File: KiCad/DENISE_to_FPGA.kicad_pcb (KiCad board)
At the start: 2 copper layers, 76.7 x 29.5 mm, 17 parts, among them J1 Conn_01x02, J2 Conn_01x02, J3 Conn_01x40, U1 LM1117-3.3, U2 74LVC245A, U3 74LVC245A, U4 74LVC1G86, U5 Denise_MB_PinHeader

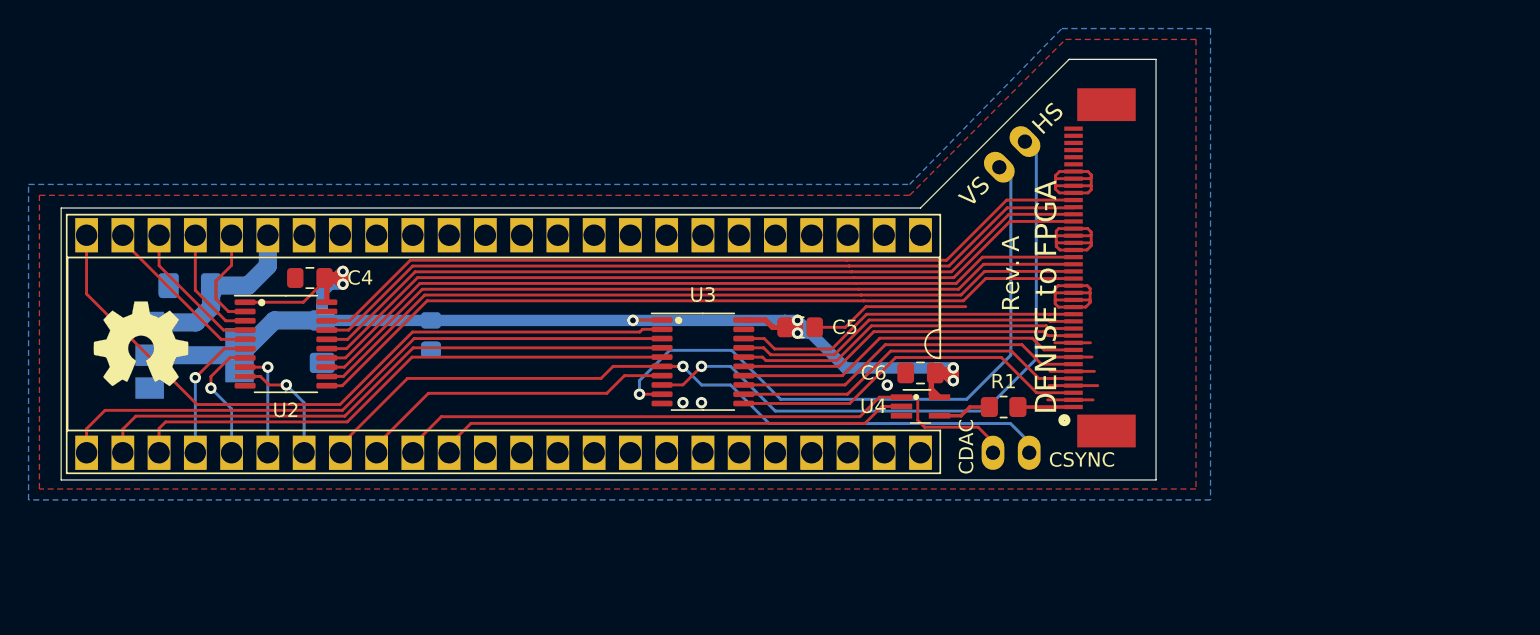
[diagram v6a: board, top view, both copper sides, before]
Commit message: Updated design with a 74LVC162244ADGG, changed PCB size and TH-pins
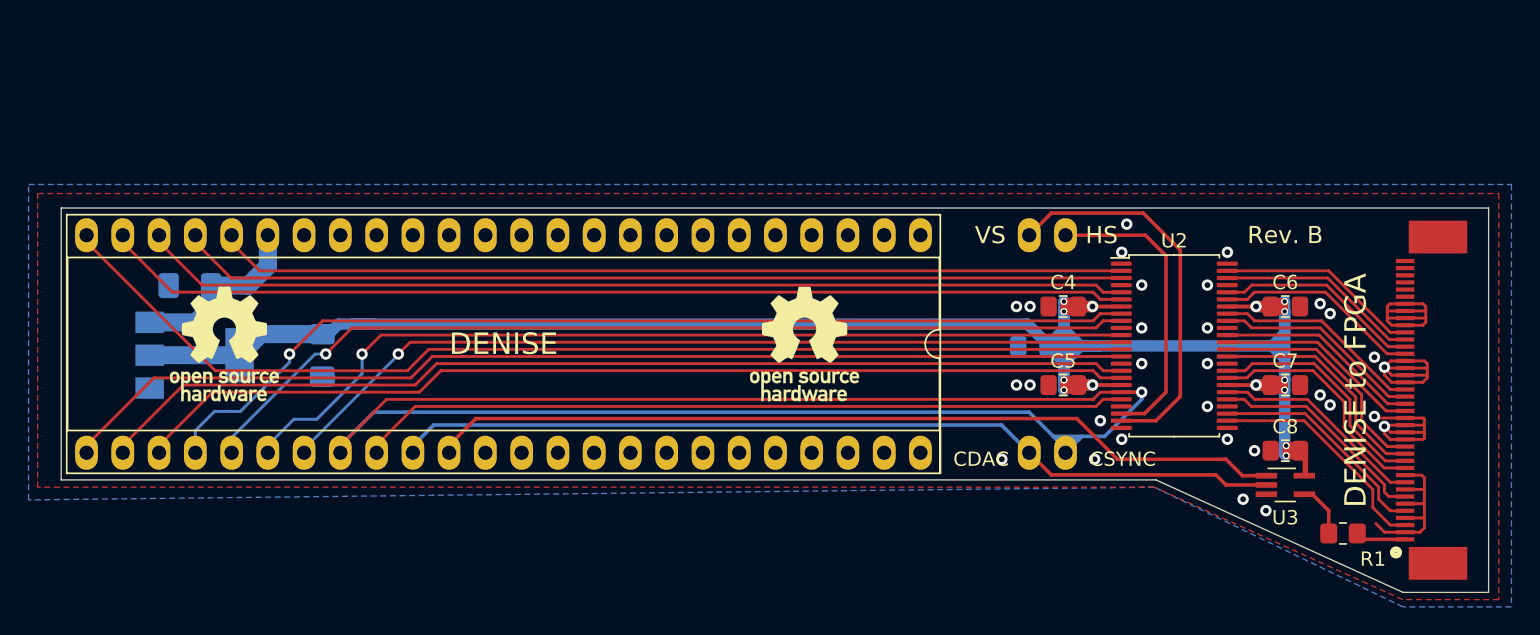
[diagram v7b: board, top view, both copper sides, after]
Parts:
- removed the REF** at (133.3, 95.8)
- removed the U4 at (188.0, 100.1)
- added C7: 0.1uF, DENISE_to_FPGA:C_0805_2012Metric_Pad1.15x1.4mm_HandSolder, F.Cu at (213.5, 98.6)
- added C8: 0.1uF, DENISE_to_FPGA:C_0805_2012Metric_Pad1.15x1.4mm_HandSolder, F.Cu at (213.5, 103.2)
- added REF**: OSHW-Logo_7.5x8mm_SilkScreen, Symbol:OSHW-Logo_7.5x8mm_SilkScreen, F.Cu at (179.8, 95.8)
- added REF**: OSHW-Logo_7.5x8mm_SilkScreen, Symbol:OSHW-Logo_7.5x8mm_SilkScreen, F.Cu at (139.2, 95.8)
- C3: value 0.1uF -> 1uF
- C4, C5: footprint Capacitor_SMD:C_0805_2012Metric_Pad1.15x1.40mm_HandSolder -> DENISE_to_FPGA:C_0805_2012Metric_Pad1.15x1.4mm_HandSolder
- C6: footprint Capacitor_SMD:C_0805_2012Metric_Pad1.18x1.45mm_HandSolder -> DENISE_to_FPGA:C_0805_2012Metric_Pad1.15x1.4mm_HandSolder
- U2: value 74LVC245A -> 74LVC162244A; footprint Package_SO:TSSOP-20_4.4x6.5mm_P0.65mm -> Package_SO:TSSOP-48_6.1x12.5mm_P0.5mm
- U3: value 74LVC245A -> 74LVC1G86; footprint Package_SO:TSSOP-20_4.4x6.5mm_P0.65mm -> Package_TO_SOT_SMD:SOT-353_SC-70-5_Handsoldering
- moved U2 62.2 mm to (205.7, 95.9)
- moved C4 52.8 mm to (198.0, 93.1)
- moved C3 42.2 mm to (195.8, 95.9), turned to 0 degrees
- moved U3 41.7 mm to (213.5, 105.6)
- moved C6 26.0 mm to (213.5, 93.1), turned to 180 degrees
- moved R1 25.4 mm to (217.6, 109.0)
- moved J3 25.0 mm to (223.8, 99.7)
- moved REF** 24.9 mm to (220.4, 98.9)
- moved C5 18.9 mm to (198.0, 98.6), turned to 0 degrees
- moved J2 5.20 mm to (195.6, 88.1), turned to 90 degrees
- moved J1 2.54 mm to (198.1, 103.4)
- moved C2 0.96 mm to (146.1, 96.6)
- renumbered U5 to U4
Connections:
- U2 pad 1: 3V3 -> GND
- U2 pad 11: G3_3V3 -> G2
- U2 pad 12: G2_3V3 -> G3
- U2 pad 13: G1_3V3 -> B0
- U2 pad 14: G0_3V3 -> B1
- U2 pad 15: R3_3V3 -> GND
- U2 pad 16: R2_3V3 -> B2
- U2 pad 17: R1_3V3 -> B3
- U2 pad 18: R0_3V3 -> 3V3
- U2 pad 19: GND -> CSYNC
- U2 pad 20: 3V3 -> PIXELSW
- U2 pad 4: R2 -> GND
- U2 pad 5: R3 -> R2
- U2 pad 6: G0 -> R3
- U2 pad 7: G1 -> 3V3
- U2 pad 8: G2 -> G0
- U2 pad 9: G3 -> G1
- U3 pad 1: 3V3 -> C7M
- U3 pad 2: B0 -> CDAC
- U3 pad 3: B1 -> GND
- U3 pad 4: B2 -> Net-(R1-Pad2)
- U3 pad 5: B3 -> 3V3
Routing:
- net CSYNC: track 54.0 -> 122.8 mm
- net 3V3: track 98.8 -> 163.4 mm, vias 7 -> 14
- net G0: track 9.59 -> 70.5 mm
- net R3: track 11.8 -> 72.2 mm
- net R2: track 10.0 -> 69.4 mm
- net R1: track 8.23 -> 66.4 mm
- net G1: track 8.87 -> 66.8 mm
- net G2: track 7.59 -> 64.3 mm
- net R0: track 7.32 -> 63.7 mm
- net G3: track 8.40 -> 60.6 mm
- net R1_3V3: track 55.9 -> 14.2 mm
- net R0_3V3: track 55.8 -> 14.2 mm
- net R3_3V3: track 56.0 -> 14.5 mm
- net R2_3V3: track 55.9 -> 14.5 mm
- net G3_3V3: track 55.4 -> 14.5 mm
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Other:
- board size 76.7 x 29.5 mm -> 100 x 26.9 mm
- board text added: "DENISE"
- board text added: "Design by J.Bilander (C) 2023, 2024"
- board text added: "Rev. B"
- board text removed: "Design by J.Bilander (C) 2023"
- board text removed: "Rev. A"

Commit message: changed U3 from 74LVC1G86 (XOR-gate, TSSOP-5) to 74LVC1G57GV (XNOR-gate, TSOP-6)
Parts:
- U3: value 74LVC1G86 -> 74LVC1G57GV; footprint Package_TO_SOT_SMD:SOT-353_SC-70-5_Handsoldering -> Package_SO:TSOP-6_1.65x3.05mm_P0.95mm
- moved U3 0.90 mm to (213.6, 106.5), turned to 90 degrees
- moved C8 0.50 mm to (213.5, 102.7), turned to 180 degrees
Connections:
- U3 pad 1: C7M -> CDAC
- U3 pad 2: CDAC -> GND
- U3 pad 3: GND -> CDAC
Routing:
- net CDAC: track 62.6 -> 67.6 mm
- net 3V3: track 163.4 -> 166.7 mm
- net C7M: track 60.2 -> 61.0 mm
- net Net-(R1-Pad2): track 3.79 -> 4.50 mm
- net GND: vias 30 -> 33
